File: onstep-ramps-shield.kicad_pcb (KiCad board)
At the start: 2 copper layers, 114.3 x 67.3 mm, 29 parts

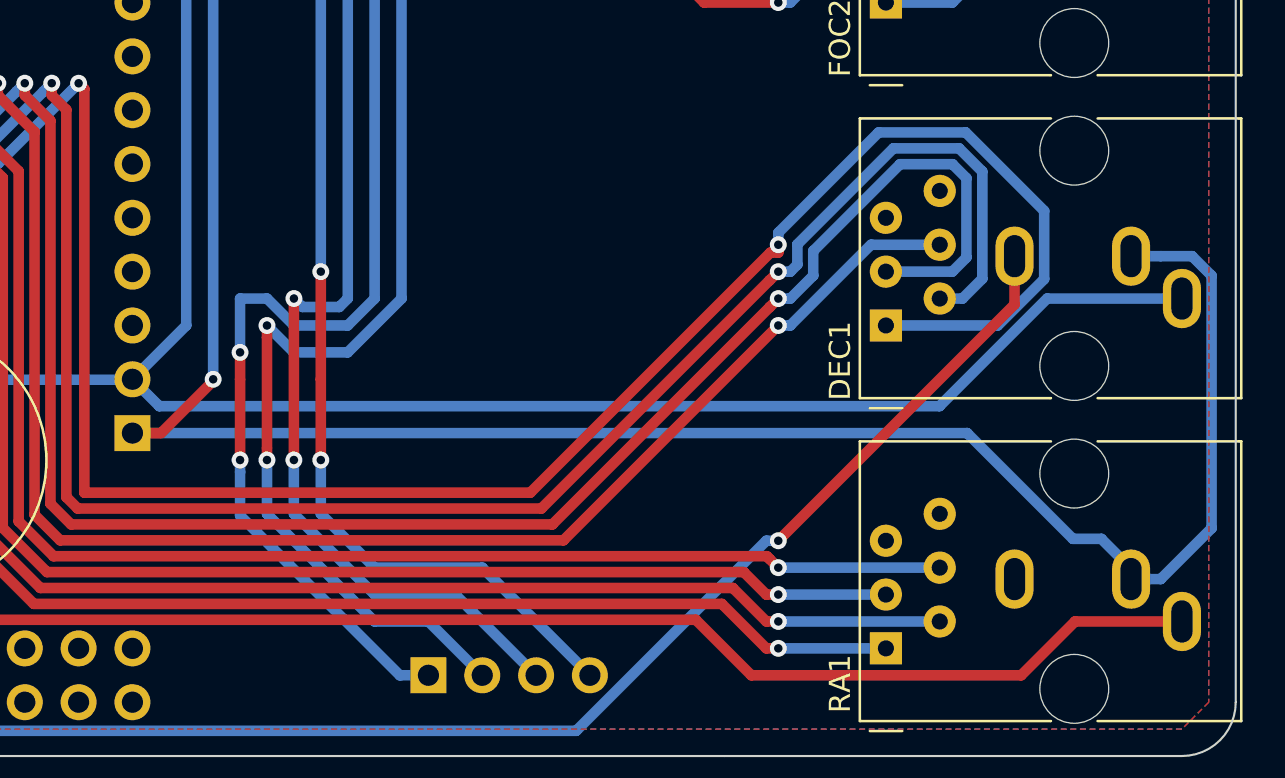
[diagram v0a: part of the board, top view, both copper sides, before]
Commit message: Update connectors
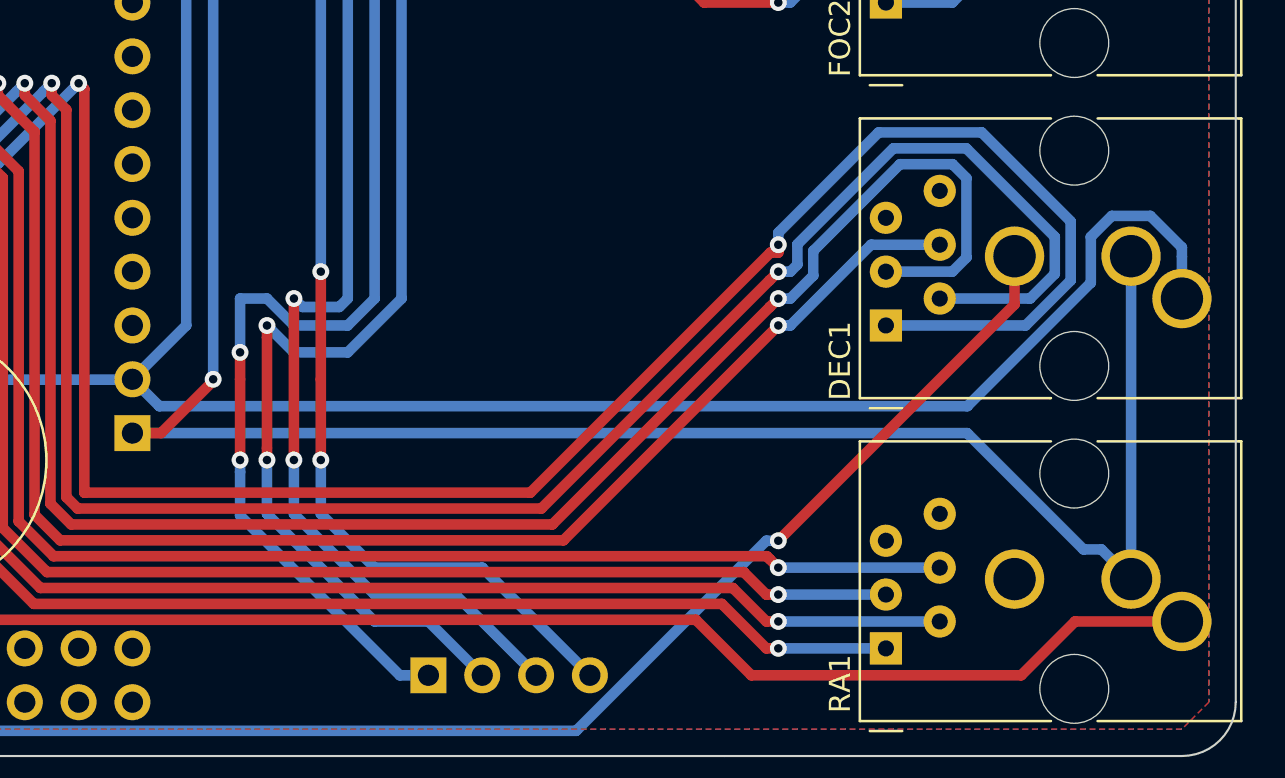
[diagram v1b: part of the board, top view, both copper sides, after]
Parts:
- J_PEC1, J_RET1: footprint Connector_Audio:Jack_3.5mm_CUI_SJ1-3533NG_Horizontal -> Connector_Audio:Jack_3.5mm_CUI_SJ1-3533NG_Horizontal_CircularHoles
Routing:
- net GND: track 123.4 -> 129.3 mm
- net VCC: track 136.5 -> 131.1 mm
- net Y_2A: track 112.8 -> 117.7 mm
- net Y_2B: track 124.7 -> 126.9 mm

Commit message: Add voltage divider for HC05
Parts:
- added R4: 1k, Resistor_SMD:R_0603_1608Metric_Pad1.05x0.95mm_HandSolder, B.Cu at (160.0, 54.6)
- added R5: 2k, Resistor_SMD:R_0603_1608Metric_Pad1.05x0.95mm_HandSolder, B.Cu at (155.3, 54.6)
- renumbered J_HC05 to J_HC5
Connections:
- J_HC5 pad 1: TX1 -> Net-(J_HC5-Pad1)
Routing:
- net TX1: track 30.8 -> 26.2 mm
- net Net-(J_HC5-Pad1): track 0.00 -> 4.20 mm
- net GND: track 129.3 -> 131.8 mm
- net RX1: track 36.6 -> 37.2 mm
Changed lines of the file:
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@@
     (thickness 1.6002)
     (drawings 29)
-    (tracks 486)
+    (tracks 492)
     (zones 0)
-    (modules 29)
-    (nets 35)
+    (modules 31)
+    (nets 36)
   )
   (page A4)
@@
   (net 33 VCC_I2C1)
   (net 34 GND_I2C1)
+  (net 35 "Net-(J_HC5-Pad1)")
   (net_class Default "This is the default net class."
     (clearance 0.25)
@@
     (add_net "Net-(D1-Pad2)")
     (add_net "Net-(D2-Pad2)")
+    (add_net "Net-(J_HC5-Pad1)")
     (add_net "Net-(J_RET1-PadS)")
     (add_net PEC1)
@@
     (diff_pair_width 0.12)
     (diff_pair_gap 0.12)
+  )
+  (module Resistor_SMD:R_0603_1608Metric_Pad1.05x0.95mm_HandSolder (layer Back)
+    (at 155.335 54.61 180)
+    (descr "Resistor SMD 0603 (1608 Metric), square (rectangular) end terminal, IPC_7351 nominal with elongated pad for handsoldering. (Body size source: http://www.tortai-tech.com/upload/download/2011102023233369053.pdf), generated with kicad-footprint-generator")
+    (tags "resistor handsolder")
+    (attr smd)
+    (fp_text reference R5 (at 0 1.43) (layer B.SilkS)
+      (effects (font (size 1 1) (thickness 0.15)) (justify mirror))
+    )
+    (fp_text value 2k (at 0 -1.43) (layer B.Fab)
+      (effects (font (size 1 1) (thickness 0.15)) (justify mirror))
+    )
+    (fp_text user %R (at 0 0) (layer B.Fab)
+      (effects (font (size 0.4 0.4) (thickness 0.06)) (justify mirror))
+    )
+    (fp_line (start 1.65 -0.73) (end -1.65 -0.73) (layer B.CrtYd) (width 0.05))
+    (fp_line (start 1.65 0.73) (end 1.65 -0.73) (layer B.CrtYd) (width 0.05))
+    (fp_line (start -1.65 0.73) (end 1.65 0.73) (layer B.CrtYd) (width 0.05))
+    (fp_line (start -1.65 -0.73) (end -1.65 0.73) (layer B.CrtYd) (width 0.05))
+    (fp_line (start -0.171267 -0.51) (end 0.171267 -0.51) (layer B.SilkS) (width 0.12))
+    (fp_line (start -0.171267 0.51) (end 0.171267 0.51) (layer B.SilkS) (width 0.12))
+    (fp_line (start 0.8 -0.4) (end -0.8 -0.4) (layer B.Fab) (width 0.1))
+    (fp_line (start 0.8 0.4) (end 0.8 -0.4) (layer B.Fab) (width 0.1))
+    (fp_line (start -0.8 0.4) (end 0.8 0.4) (layer B.Fab) (width 0.1))
+    (fp_line (start -0.8 -0.4) (end -0.8 0.4) (layer B.Fab) (width 0.1))
+    (pad 2 smd roundrect (at 0.875 0 180) (size 1.05 0.95) (layers Back B.Paste B.Mask) (roundrect_rratio 0.25)
+      (net 14 GND))
+    (pad 1 smd roundrect (at -0.875 0 180) (size 1.05 0.95) (layers Back B.Paste B.Mask) (roundrect_rratio 0.25)
+      (net 27 TX1))
+    (model ${KISYS3DMOD}/Resistor_SMD.3dshapes/R_0603_1608Metric.wrl
+      (at (xyz 0 0 0))
+      (scale (xyz 1 1 1))
+      (rotate (xyz 0 0 0))
+    )
+  )
+  (module Resistor_SMD:R_0603_1608Metric_Pad1.05x0.95mm_HandSolder (layer Back)
+    (at 160.02 54.61)
+    (descr "Resistor SMD 0603 (1608 Metric), square (rectangular) end terminal, IPC_7351 nominal with elongated pad for handsoldering. (Body size source: http://www.tortai-tech.com/upload/download/2011102023233369053.pdf), generated with kicad-footprint-generator")
+    (tags "resistor handsolder")
+    (attr smd)
+    (fp_text reference R4 (at 0 1.43) (layer B.SilkS)
+      (effects (font (size 1 1) (thickness 0.15)) (justify mirror))
+    )
+    (fp_text value 1k (at 0 -1.43) (layer B.Fab)
+      (effects (font (size 1 1) (thickness 0.15)) (justify mirror))
+    )
+    (fp_text user %R (at 0 0) (layer B.Fab)
+      (effects (font (size 0.4 0.4) (thickness 0.06)) (justify mirror))
+    )
+    (fp_line (start 1.65 -0.73) (end -1.65 -0.73) (layer B.CrtYd) (width 0.05))
+    (fp_line (start 1.65 0.73) (end 1.65 -0.73) (layer B.CrtYd) (width 0.05))
+    (fp_line (start -1.65 0.73) (end 1.65 0.73) (layer B.CrtYd) (width 0.05))
+    (fp_line (start -1.65 -0.73) (end -1.65 0.73) (layer B.CrtYd) (width 0.05))
+    (fp_line (start -0.171267 -0.51) (end 0.171267 -0.51) (layer B.SilkS) (width 0.12))
+    (fp_line (start -0.171267 0.51) (end 0.171267 0.51) (layer B.SilkS) (width 0.12))
+    (fp_line (start 0.8 -0.4) (end -0.8 -0.4) (layer B.Fab) (width 0.1))
+    (fp_line (start 0.8 0.4) (end 0.8 -0.4) (layer B.Fab) (width 0.1))
+    (fp_line (start -0.8 0.4) (end 0.8 0.4) (layer B.Fab) (width 0.1))
+    (fp_line (start -0.8 -0.4) (end -0.8 0.4) (layer B.Fab) (width 0.1))
+    (pad 2 smd roundrect (at 0.875 0) (size 1.05 0.95) (layers Back B.Paste B.Mask) (roundrect_rratio 0.25)
+      (net 35 "Net-(J_HC5-Pad1)"))
+    (pad 1 smd roundrect (at -0.875 0) (size 1.05 0.95) (layers Back B.Paste B.Mask) (roundrect_rratio 0.25)
+      (net 27 TX1))
+    (model ${KISYS3DMOD}/Resistor_SMD.3dshapes/R_0603_1608Metric.wrl
+      (at (xyz 0 0 0))
+      (scale (xyz 1 1 1))
+      (rotate (xyz 0 0 0))
+    )
   )
   (module Connector_Audio:Jack_3.5mm_CUI_SJ1-3533NG_Horizontal_CircularHoles (layer Back)
@@
     (descr "Through hole straight socket strip, 1x04, 2.54mm pitch, single row (from Kicad 4.0.7), script generated")
     (tags "Through hole socket strip THT 1x04 2.54mm single row")
-    (fp_text reference J_HC05 (at 2.54 1.27 180) (layer F.SilkS)
+    (fp_text reference J_HC5 (at 2.54 1.27 180) (layer F.SilkS)
       (effects (font (size 1 1) (thickness 0.15)))
     )
@@
       (net 26 RX1))
     (pad 1 thru_hole rect (at 0 0 90) (size 1.7 1.7) (drill 1) (layers *.Cu *.Mask)
-      (net 27 TX1))
+      (net 35 "Net-(J_HC5-Pad1)"))
     (model ${KISYS3DMOD}/Connector_PinSocket_2.54mm.3dshapes/PinSocket_1x04_P2.54mm_Vertical.wrl
       (at (xyz 0 0 0))
@@
   (segment (start 196.359999 93.607999) (end 197.347999 92.619999) (width 0.5) (layer Back) (net 14))
   (segment (start 190.534998 101.6) (end 196.359999 95.774999) (width 0.5) (layer Back) (net 14))
+  (segment (start 155.335001 55.960001) (end 156.129999 55.960001) (width 0.5) (layer Back) (net 14))
+  (segment (start 154.46 55.085) (end 155.335001 55.960001) (width 0.5) (layer Back) (net 14))
+  (segment (start 154.46 54.61) (end 154.46 55.085) (width 0.5) (layer Back) (net 14))
   (segment (start 189.23 109.22) (end 181.61 109.22) (width 0.5) (layer Back) (net 15))
   (via (at 181.61 109.22) (size 0.8) (drill 0.4) (layers Front Back) (net 15))
@@
   (segment (start 156.21 96.52) (end 157.48 96.52) (width 0.5) (layer Back) (net 25))
   (segment (start 156.21 99.06) (end 156.21 96.52) (width 0.5) (layer Back) (net 25))
+  (segment (start 167.64 54.61) (end 165.619989 52.589989) (width 0.5) (layer Back) (net 26))
+  (segment (start 147.990011 52.589989) (end 137.16 63.42) (width 0.5) (layer Back) (net 26))
+  (segment (start 165.619989 52.589989) (end 147.990011 52.589989) (width 0.5) (layer Back) (net 26))
   (segment (start 137.16 63.42) (end 137.16 64.77) (width 0.5) (layer Back) (net 26))
-  (segment (start 147.320001 53.259999) (end 137.16 63.42) (width 0.5) (layer Back) (net 26))
-  (segment (start 166.289999 53.259999) (end 147.320001 53.259999) (width 0.5) (layer Back) (net 26))
-  (segment (start 167.64 54.61) (end 166.289999 53.259999) (width 0.5) (layer Back) (net 26))
-  (segment (start 139.7 63.567919) (end 139.7 64.77) (width 0.5) (layer Back) (net 27))
-  (segment (start 139.7 62.771998) (end 139.7 63.567919) (width 0.5) (layer Back) (net 27))
-  (segment (start 147.861998 54.61) (end 139.7 62.771998) (width 0.5) (layer Back) (net 27))
-  (segment (start 165.1 54.61) (end 147.861998 54.61) (width 0.5) (layer Back) (net 27))
+  (segment (start 156.21 54.135) (end 156.21 54.61) (width 0.5) (layer Back) (net 27))
+  (segment (start 155.415 53.34) (end 156.21 54.135) (width 0.5) (layer Back) (net 27))
+  (segment (start 149.131998 53.34) (end 155.415 53.34) (width 0.5) (layer Back) (net 27))
+  (segment (start 139.7 62.771998) (end 149.131998 53.34) (width 0.5) (layer Back) (net 27))
+  (segment (start 139.7 64.77) (end 139.7 62.771998) (width 0.5) (layer Back) (net 27))
+  (segment (start 159.145 54.61) (end 156.21 54.61) (width 0.5) (layer Back) (net 27))
   (segment (start 106.205 116.05) (end 106.68 116.05) (width 0.5) (layer Front) (net 28))
   (segment (start 105.70499 111.326988) (end 105.70499 115.54999) (width 0.5) (layer Front) (net 28))
@@
   (segment (start 160.101404 64.768596) (end 165.1 59.77) (width 0.5) (layer Back) (net 34))
   (segment (start 156.211404 64.768596) (end 160.101404 64.768596) (width 0.5) (layer Back) (net 34))
+  (segment (start 160.895 54.61) (end 165.1 54.61) (width 0.5) (layer Back) (net 35))
   (zone (net 0) (net_name "") (layer Front) (hatch edge 0.508)
     (connect_pads (clearance 0.508))

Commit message: Re-route R4 trace
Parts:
- added REF**: OSHW-Logo2_7.3x6mm_SilkScreen, Symbol:OSHW-Logo2_7.3x6mm_SilkScreen, F.Cu at (94.0, 55.9)
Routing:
- net GND: track 131.8 -> 132.5 mm

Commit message: Rearrange resistors
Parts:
- removed REF**: OSHW-Logo2_7.3x6mm_SilkScreen, Symbol:OSHW-Logo2_7.3x6mm_SilkScreen
- moved R5 6.02 mm to (161.3, 53.7), turned to 270 degrees
- moved BZ1 5.08 mm to (141.0, 102.9)
- moved R4 2.69 mm to (157.5, 53.7), turned to 270 degrees
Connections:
- R4 pad 1: TX1 -> Net-(J_HC5-Pad1)
- R4 pad 2: Net-(J_HC5-Pad1) -> TX1
- R5 pad 1: TX1 -> Net-(J_HC5-Pad1)
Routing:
- net Net-(J_HC5-Pad1): track 4.20 -> 8.34 mm
- net BUZZER1: track 39.2 -> 42.1 mm
- net TX1: track 26.2 -> 24.2 mm
- net RX1: track 37.2 -> 37.8 mm
- net GND: track 132.5 -> 131.9 mm

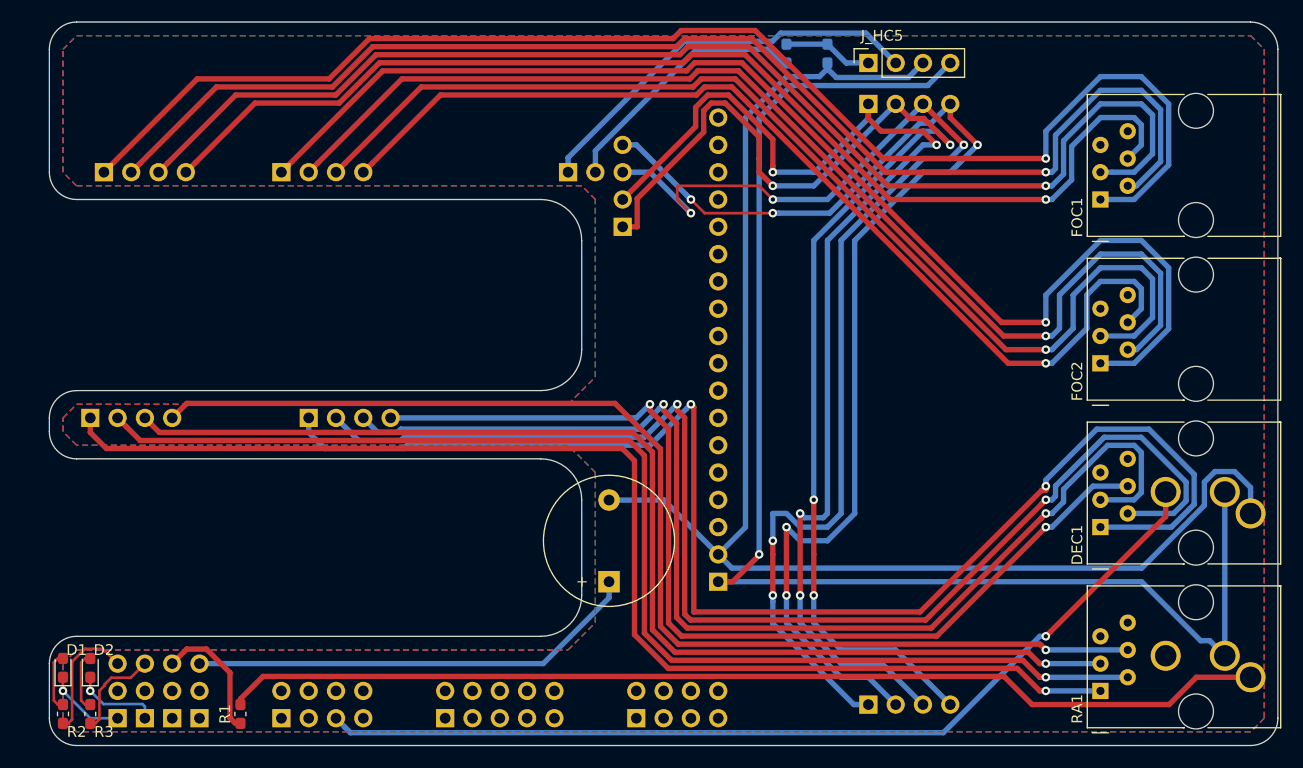
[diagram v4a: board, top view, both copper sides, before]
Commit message: Increase trace to edge distance for LEDs
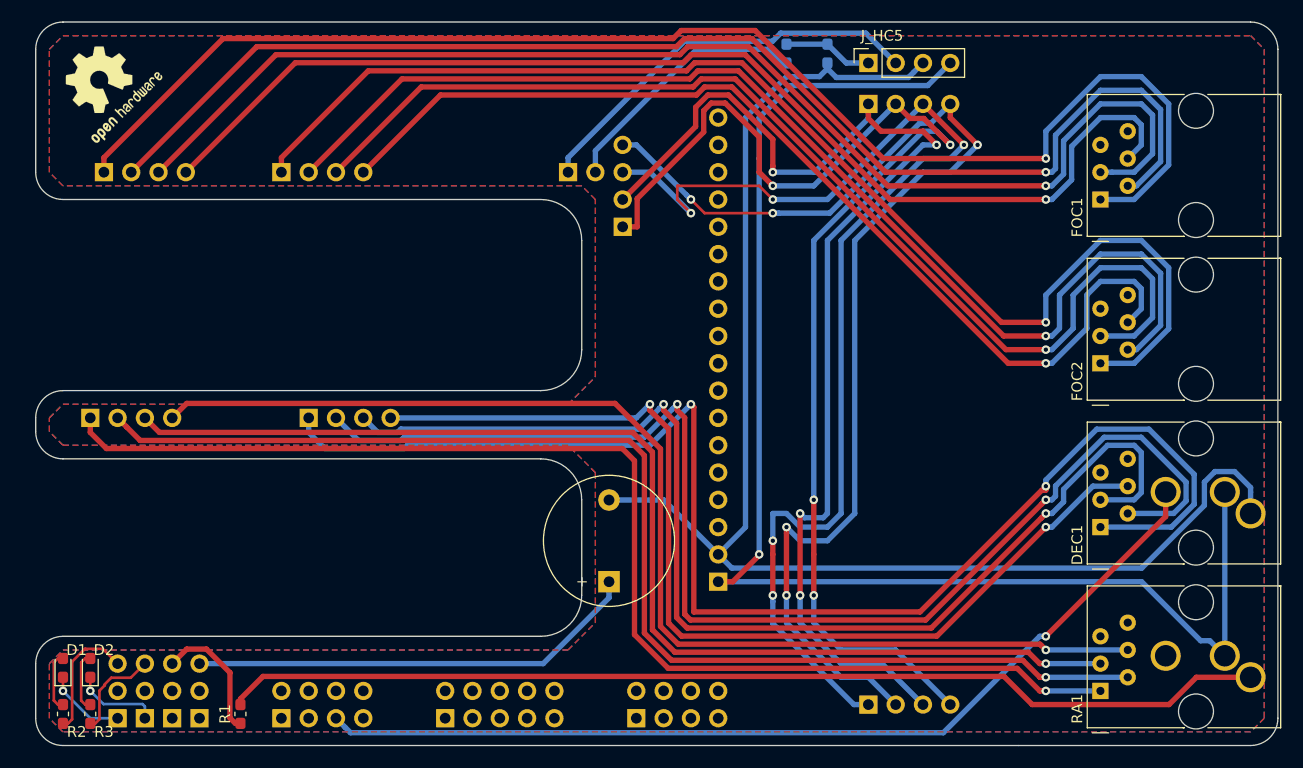
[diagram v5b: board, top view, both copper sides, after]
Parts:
- added REF**: OSHW-Logo2_9.8x8mm_SilkScreen, Symbol:OSHW-Logo2_9.8x8mm_SilkScreen, F.Cu at (94.0, 56.6)
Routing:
- net E1_2B: track 115.8 -> 116.6 mm
- net E0_2B: track 128.5 -> 129.3 mm
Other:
- board size 114.3 x 67.3 mm -> 115.6 x 67.3 mm

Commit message: Increased connector distance
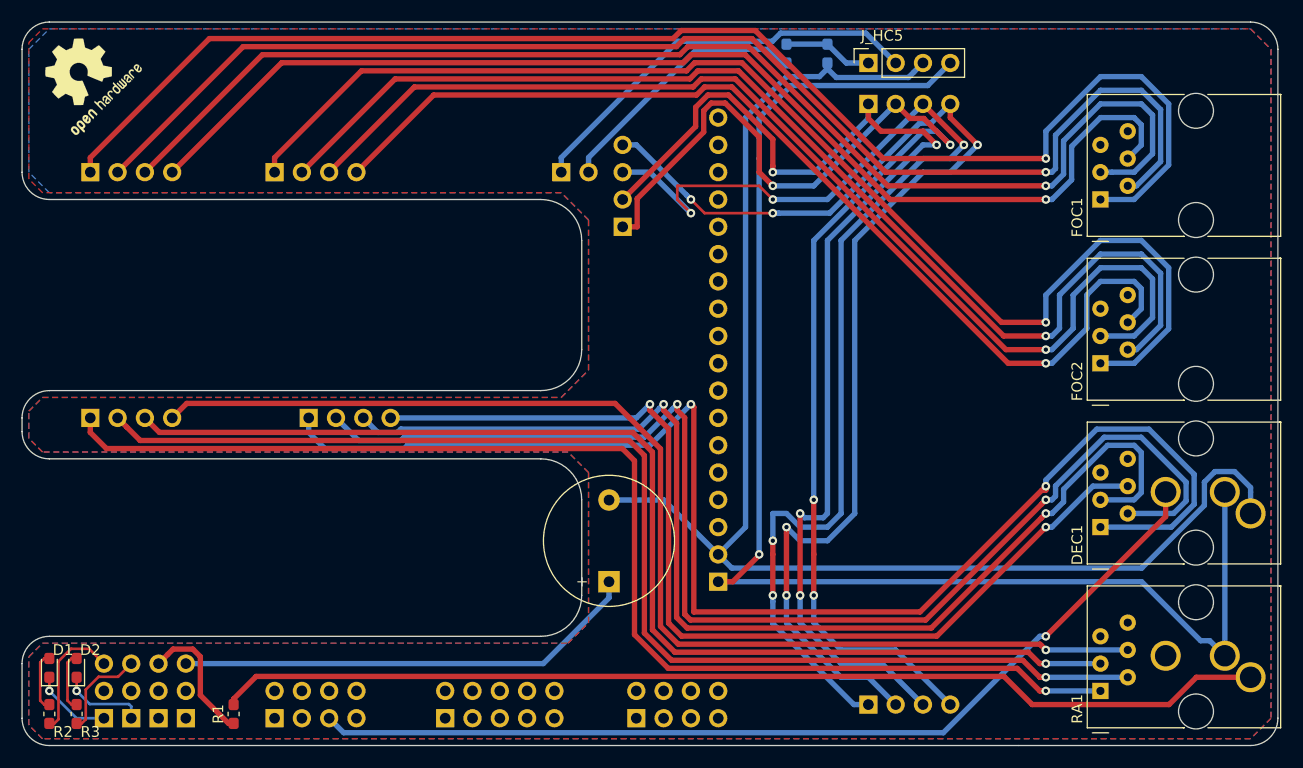
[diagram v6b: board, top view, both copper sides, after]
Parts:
- moved REF** 2.04 mm to (92.1, 55.9)
- moved J_FOC1 1.27 mm to (92.7, 64.8)
- moved J_SERV2 1.27 mm to (96.5, 115.6)
- moved J_SERV4 1.27 mm to (101.6, 115.6)
- moved D1 1.27 mm to (88.9, 110.9)
- moved D2 1.27 mm to (91.4, 110.9)
- moved J_SERV1 1.27 mm to (94.0, 115.6)
- moved J_SERV3 1.27 mm to (99.1, 115.6)
- moved R2 1.27 mm to (88.9, 115.2)
- moved R3 1.27 mm to (91.4, 115.2)
- moved R1 0.64 mm to (106.0, 115.2)
- moved J_AUX1 0.63 mm to (109.9, 115.6)
- moved J_FOC2 0.63 mm to (109.9, 64.8)
- moved J_SER1 0.63 mm to (136.5, 64.8)
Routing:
- net E0_2B: track 129.3 -> 130.6 mm
- net E0_2A: track 120.6 -> 121.9 mm
- net E0_1A: track 117.2 -> 118.5 mm
- net BUZZER1: track 42.1 -> 43.4 mm
- net E0_1B: track 107.9 -> 109.2 mm
- net PEC1: track 88.4 -> 89.0 mm
- net Net-(J_RET1-PadS): track 97.5 -> 98.1 mm
- net E1_1B: track 95.2 -> 95.9 mm
- net RX1: track 37.8 -> 38.4 mm
- net E1_2B: track 116.6 -> 117.2 mm
- net E1_2A: track 107.9 -> 108.6 mm
- net E1_1A: track 104.6 -> 105.2 mm
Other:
- board size 115.6 x 67.3 mm -> 116.8 x 67.3 mm
